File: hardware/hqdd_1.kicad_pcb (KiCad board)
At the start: 4 copper layers, 35 x 35 mm, 57 parts, among them IC1 TAR5SB33, IC2 TAR5SB33, J1 Conn_01x02, J2 Conn_01x04, J3 Conn_01x02, J4 Conn_01x02, J5 Conn_01x01_Pin, J6 Conn_01x01_Pin, J7 Conn_01x01_Pin, SW1 SKRPACE010, U1 STM32G431KBUx, U2 DRV8311H, U3 AS5600L-ASOM, U5 TCAN330

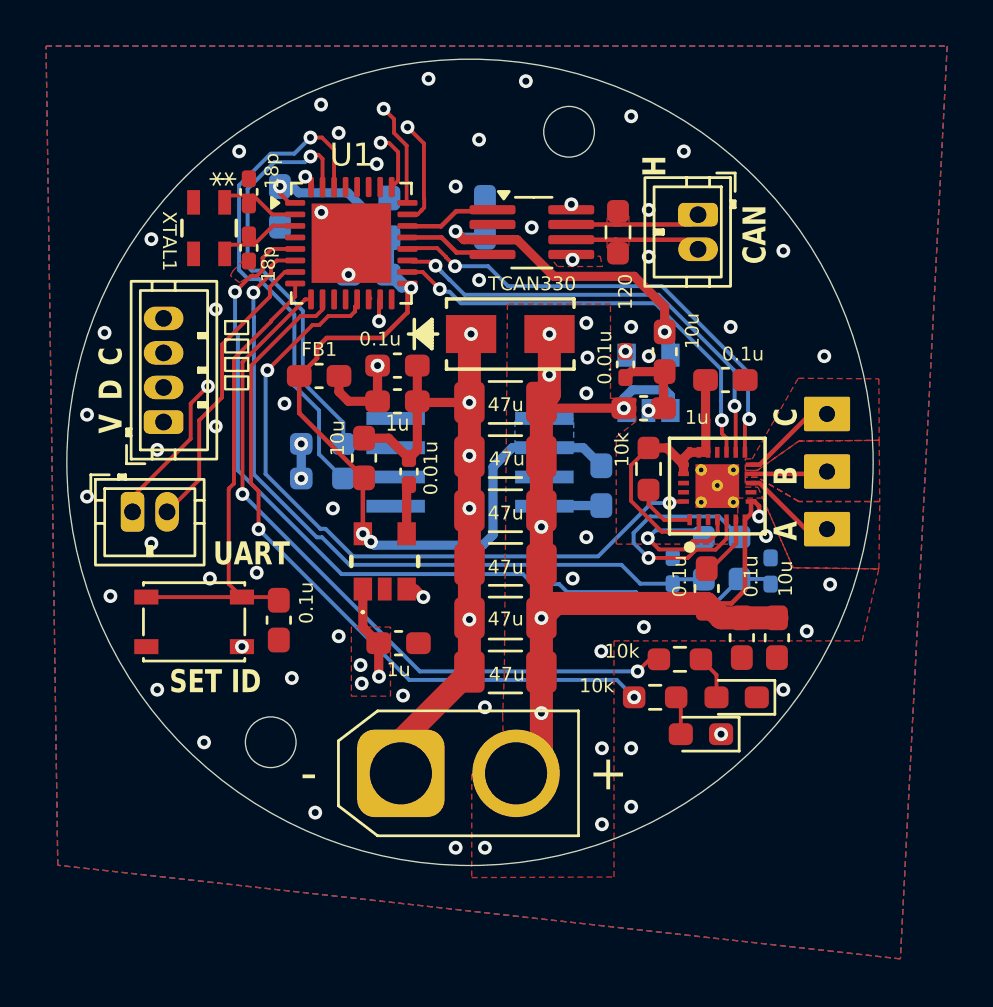
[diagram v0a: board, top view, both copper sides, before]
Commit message: PCBをデイジーチェーンに対応
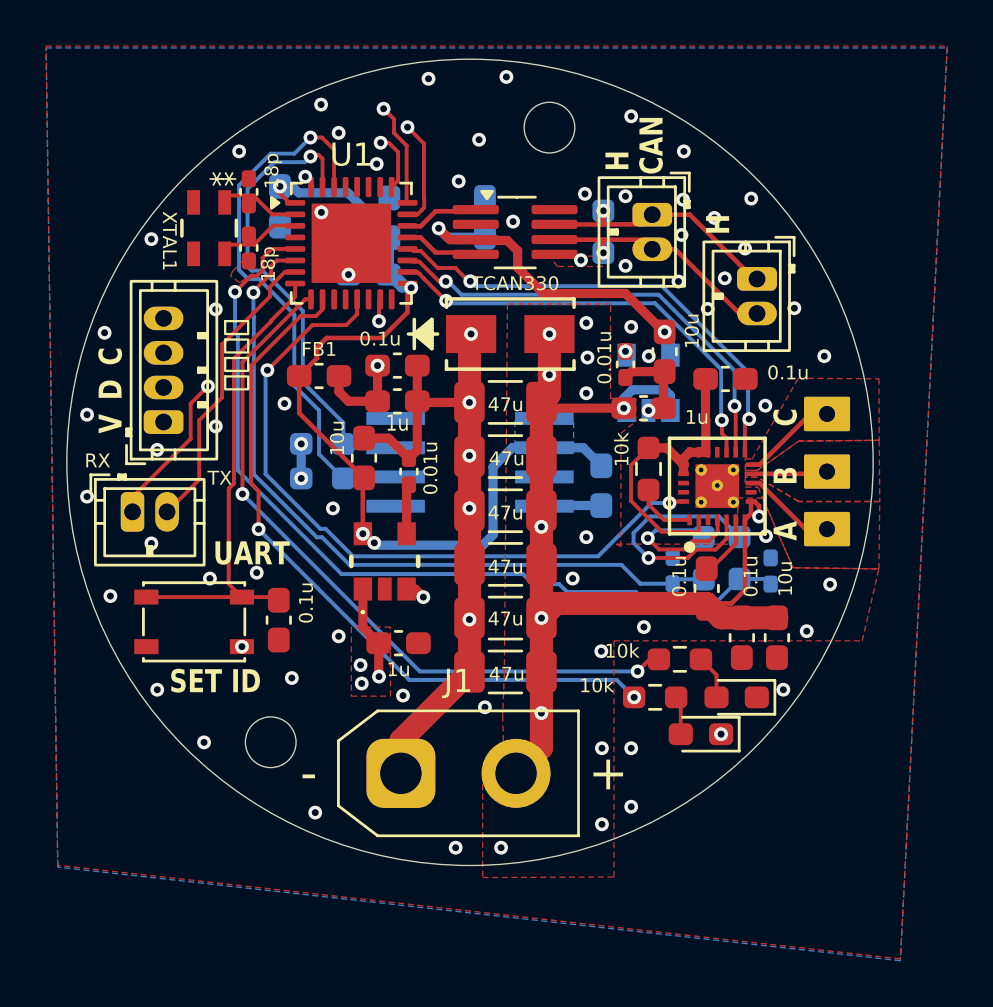
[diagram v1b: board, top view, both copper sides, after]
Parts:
- added J8: Conn_01x02, Connector_JST:JST_ZH_B2B-ZR_1x02_P1.50mm_Vertical, F.Cu at (84.7, 53.3)
- J1: footprint Connector_AMASS:AMASS_XT30U-M_1x02_P5.0mm_Vertical -> Connector_AMASS:AMASS_XT30UPB-M_1x02_P5.0mm_Vertical
- R3: moved to B.Cu
- moved J4 1.99 mm to (80.2, 50.5)
- moved REF** 0.87 mm to (75.7, 46.7)
- moved U5 0.73 mm to (74.2, 51.2)
- moved R3 0.64 mm to (78.0, 51.2)
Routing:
- net CAN_L: track 6.41 -> 10.0 mm, vias 0 -> 1
- net CAN_H: track 6.86 -> 10.00 mm, vias 0 -> 1
- net +3.3V2: track 14.0 -> 15.4 mm
- net CAN_TX: track 3.46 -> 2.90 mm
- net CAN_RX: track 3.46 -> 2.90 mm
- net GND: vias 56 -> 63
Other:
- board text added: "RX"
- board text added: "TX"
